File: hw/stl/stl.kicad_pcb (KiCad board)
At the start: 2 copper layers, 36 parts, among them Q1 IRF4905, Q2 5505, Q3 5505, Q4 5505, Q5 5505, Q6 5505, Q7 5505, Q8 5505, Q9 5505, U1 STM8S003F3P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

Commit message: WIP: tracing in progress
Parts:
- removed OUT1: Screw_Terminal_01x05, TerminalBlock_MetzConnect:TerminalBlock_MetzConnect_Type011_RT05505HBWC_1x05_P5.00mm_Horizontal
- removed Q5, Q9: 5505, Package_TO_SOT_SMD:TO-252-2
- removed R10, R14: 1K, Resistor_SMD:R_1206_3216Metric
- added D2: LED, LED_SMD:LED_1206_3216Metric, F.Cu at (216.9, 41.8)
- added J1: Screw_Terminal_01x04, TerminalBlock_Phoenix:TerminalBlock_Phoenix_MKDS-1,5-4_1x04_P5.00mm_Horizontal, F.Cu at (270.6, 27.8)
- added R15: 68, Resistor_SMD:R_1206_3216Metric, B.Cu at (221.4, 37.8)
- C1, C2, C3, C4, C5, Q4, Q7, R1, R11, R12, R13, R2, R3, R4, R6, U2: moved to B.Cu
- Q2: value 5505 -> IRFR5505TRLPBF; moved to B.Cu
- moved Q4 116.4 mm to (254.0, 46.7)
- moved Q2 104.7 mm to (254.0, 29.0)
- moved R12 96.1 mm to (245.5, 36.8), turned to 90 degrees
- moved SWIM1 93.1 mm to (210.6, 21.0)
- moved R8 92.0 mm to (245.5, 38.7), turned to 270 degrees
- moved R13 87.8 mm to (245.5, 45.8), turned to 90 degrees
- moved U2 83.9 mm to (200.4, 31.0), turned to 90 degrees
- moved Q3 83.5 mm to (254.0, 37.8)
- moved R2 82.9 mm to (225.4, 23.7)
- moved Q7 82.9 mm to (254.0, 37.7)
- moved C5 82.6 mm to (206.9, 32.1), turned to 270 degrees
- moved R6 81.3 mm to (220.0, 33.9), turned to 90 degrees
- moved R7 71.4 mm to (245.5, 30.0), turned to 270 degrees
- moved Q6 71.1 mm to (254.0, 29.1)
- moved Q1 68.7 mm to (199.4, 35.1)
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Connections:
- Q2 pad 1: +12V -> lamp2_ctrl
- Q2 pad 2: lamp2_ctrl -> lamp2_out
- Q2 pad 3: lamp2_out -> +12V
- Q3 pad 1: +12V -> lamp3_ctrl
- Q3 pad 2: lamp3_ctrl -> lamp3_out
- Q3 pad 3: lamp3_out -> +12V
- Q4 pad 1: +12V -> lamp4_ctrl
- Q4 pad 2: lamp4_ctrl -> lamp4_out
- Q4 pad 3: lamp4_out -> +12V
- Q6 pad 1: +12V -> lamp2_ctrl
- Q6 pad 2: lamp2_ctrl -> lamp2_out
- Q6 pad 3: lamp2_out -> +12V
- Q7 pad 1: +12V -> lamp3_ctrl
- Q7 pad 2: lamp3_ctrl -> lamp3_out
- Q7 pad 3: lamp3_out -> +12V
- Q8 pad 1: +12V -> lamp4_ctrl
- Q8 pad 2: lamp4_ctrl -> lamp4_out
- Q8 pad 3: lamp4_out -> +12V
- U1 pad 10: HEART_BEAT -> Net-(D2-Pad2)
- U1 pad 16: L5_STM_OUT -> Net-(U1-Pad16)
- U3 pad 1: L2_STM_OUT -> L4_STM_OUT
- U3 pad 11: Net-(U3-Pad11) -> lamp4_ctrl
- U3 pad 12: Net-(U3-Pad12) -> lamp4_ctrl
- U3 pad 13: lamp5_ctrl -> lamp3_ctrl
- U3 pad 14: lamp4_ctrl -> lamp3_ctrl
- U3 pad 15: lamp3_ctrl -> lamp2_ctrl
- U3 pad 2: L3_STM_OUT -> L4_STM_OUT
- U3 pad 3: L4_STM_OUT -> L3_STM_OUT
- U3 pad 4: L5_STM_OUT -> L3_STM_OUT
- U3 pad 5: GND -> L2_STM_OUT
- U3 pad 6: GND -> L2_STM_OUT
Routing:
- net +3V3: track 0.00 -> 14.1 mm, vias 0 -> 1
- net L4_STM_OUT: track 0.00 -> 12.7 mm
- net L3_STM_OUT: track 0.00 -> 12.5 mm
- net L2_STM_OUT: track 0.00 -> 11.7 mm
- net lamp2_ctrl: track 0.00 -> 11.2 mm
- net lamp4_ctrl: track 0.00 -> 11.1 mm
- net lamp3_ctrl: track 0.00 -> 11.1 mm
- net LEARN: track 0.00 -> 9.13 mm
- net Net-(D2-Pad1): track 0.00 -> 7.39 mm, vias 0 -> 1
- net Net-(C1-Pad2): track 0.00 -> 5.58 mm, vias 0 -> 1
- net Net-(D2-Pad2): track 0.00 -> 3.56 mm
- net CNT1: track 0.00 -> 2.96 mm, vias 0 -> 1
- net CNT2: track 0.00 -> 2.94 mm, vias 0 -> 1
- net NRST: track 0.00 -> 2.71 mm
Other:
- net class signalling added: clearance 0.2, trace_width 0.5, via_dia 0.8, via_drill 0.4

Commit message: WIP: draft tracing
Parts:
- moved R2 5.98 mm to (231.1, 25.3), turned to 180 degrees
- moved R1 5.97 mm to (225.4, 25.3), turned to 180 degrees
- moved J1 5.67 mm to (266.3, 24.2)
- moved R11 5.67 mm to (241.1, 24.5)
- moved R12 5.67 mm to (241.1, 33.2)
- moved R13 5.67 mm to (241.1, 42.2)
- moved R7 5.67 mm to (241.1, 26.4)
- moved R8 5.67 mm to (241.1, 35.1)
- moved R9 5.67 mm to (241.1, 44.0)
- moved Q2 5.67 mm to (249.6, 25.3)
- moved Q3 5.67 mm to (249.6, 34.2)
- moved Q4 5.67 mm to (249.6, 43.1)
- moved Q6 5.67 mm to (249.6, 25.5)
- moved Q7 5.67 mm to (249.6, 34.1)
- moved Q8 5.67 mm to (249.6, 43.1)
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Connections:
- C4 pad 1: Net-(C4-Pad1) -> +12V
- D1 pad 1: Net-(C4-Pad1) -> +12V
- IN1 pad 1: +12V -> +BATT
- J1 pad 1: +12V -> +BATT
- Q1 pad 2: +12V -> +BATT
- Q1 pad 3: Net-(C4-Pad1) -> +12V
- U2 pad 3: Net-(C4-Pad1) -> +12V
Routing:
- net +BATT: track 0.00 -> 143.4 mm
- net +12V: track 0.00 -> 46.8 mm, vias 0 -> 18
- net lamp4_out: track 0.00 -> 32.3 mm
- net lamp2_out: track 0.00 -> 32.2 mm
- net lamp3_out: track 0.00 -> 29.1 mm
- net +3V3: track 14.1 -> 42.5 mm, vias 1 -> 0
- net CNT2: track 2.94 -> 29.7 mm, vias 1 -> 3
- net CNT1: track 2.96 -> 24.4 mm
- net lamp2_ctrl: track 11.2 -> 32.3 mm, vias 0 -> 1
- net SWIM: track 0.00 -> 19.3 mm, vias 0 -> 1
- net lamp4_ctrl: track 11.1 -> 27.7 mm, vias 0 -> 1
- net NRST: track 2.71 -> 18.9 mm
- net lamp3_ctrl: track 11.1 -> 27.0 mm, vias 0 -> 1
- added copper zone on B.Cu, net +12V
- added copper zone on F.Cu, net +12V
- added copper zone on B.Cu, net GND
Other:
- board outline added: 102 x 43.8 mm
- net class 12V added: clearance 0.2, trace_width 0.5, via_dia 0.8, via_drill 0.4
- net class 3v3 added: clearance 0.2, trace_width 0.5, via_dia 0.8, via_drill 0.4
- net class lamp added: clearance 0.2, trace_width 2, via_dia 0.8, via_drill 0.4
- net class signalling removed
- net class signals added: clearance 0.2, trace_width 0.3, via_dia 0.8, via_drill 0.4

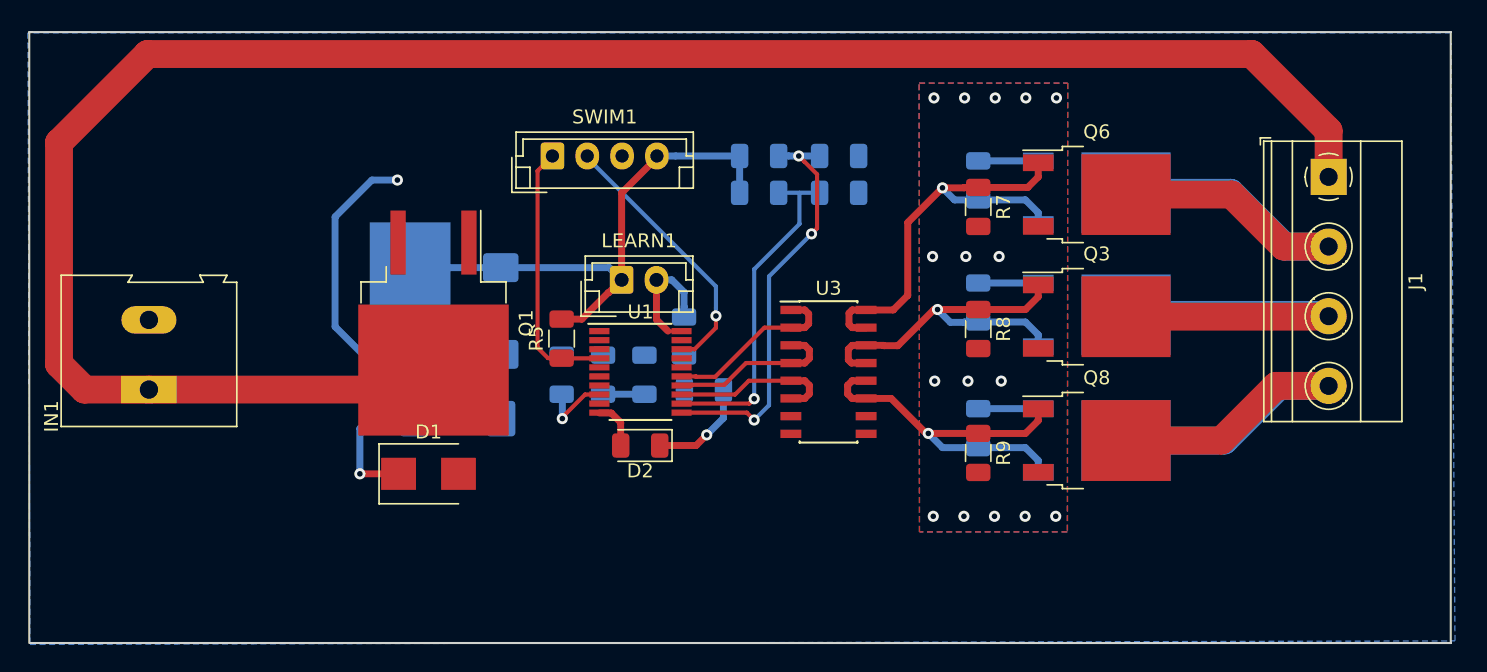
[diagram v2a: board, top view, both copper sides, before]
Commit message: [FEAT]: pcb is traced, v2.0
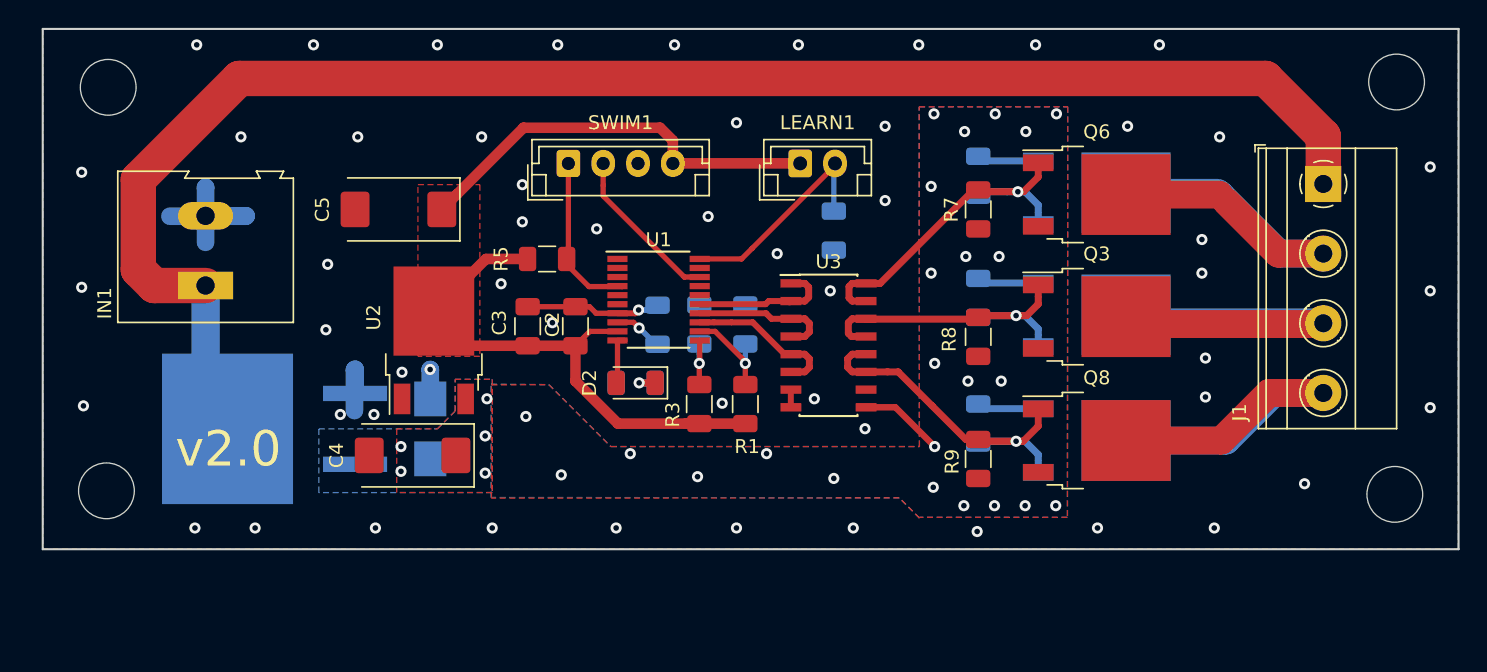
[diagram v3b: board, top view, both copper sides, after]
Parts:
- added REF**: MountingHole_4mm, MountingHole:MountingHole_4mm, F.Cu at (178.7, 17.8)
- added REF**: MountingHole_4mm, MountingHole:MountingHole_4mm, F.Cu at (178.6, 46.7)
- added REF**: MountingHole_4mm, MountingHole:MountingHole_4mm, F.Cu at (271.1, 17.4)
- added REF**: MountingHole_4mm, MountingHole:MountingHole_4mm, F.Cu at (271.0, 47.0)
- C2, C3, C4, C5, R1, R3, U2: moved to F.Cu
- D1, Q1: moved to B.Cu
- moved R3 18.3 mm to (221.1, 40.5), turned to 270 degrees
- moved R4 15.7 mm to (221.1, 34.8), turned to 270 degrees
- moved LEARN1 15.3 mm to (228.3, 23.2)
- moved R1 15.2 mm to (224.4, 40.5), turned to 270 degrees
- moved Q1 13.7 mm to (190.6, 42.3), turned to 180 degrees
- moved R6 13.2 mm to (230.8, 28.1)
- moved R2 11.6 mm to (224.4, 34.8), turned to 270 degrees
- moved C5 10.3 mm to (199.5, 26.5), turned to 180 degrees
- moved IN1 8.50 mm to (185.7, 32.0)
- moved C1 7.76 mm to (218.1, 34.8)
- moved C3 6.43 mm to (208.8, 34.9)
- moved C2 6.05 mm to (212.2, 34.9)
- moved R5 5.81 mm to (210.2, 30.1), turned to 180 degrees
- moved U1 5.34 mm to (218.2, 33.0)
- moved R15 4.93 mm to (216.5, 39.0)
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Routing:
- net GND: track 0.00 -> 30.2 mm, vias 0 -> 56
- net +3V3: track 42.5 -> 71.3 mm
- net +12V: track 46.8 -> 19.0 mm, vias 18 -> 29
- net +BATT: track 143.4 -> 115.9 mm
- net CNT2: track 29.7 -> 4.57 mm, vias 3 -> 1
- net CNT1: track 24.4 -> 7.25 mm
- net SWIM: track 19.3 -> 11.7 mm, vias 1 -> 0
- net LEARN: track 9.13 -> 16.6 mm
- net lamp2_ctrl: track 32.3 -> 26.2 mm
- net NRST: track 18.9 -> 12.9 mm
- net Net-(D2-Pad1): track 7.39 -> 2.29 mm
- net lamp3_ctrl: track 27.0 -> 23.7 mm
- net L4_STM_OUT: track 12.8 -> 10.3 mm
- net lamp4_ctrl: track 27.7 -> 25.7 mm
- net Net-(C1-Pad2): track 5.25 -> 3.35 mm
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- added copper zone on F.Cu, net +3V3
- added copper zone on F.Cu, net GND
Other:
- board size 102 x 43.8 mm -> 101.6 x 37.3 mm
- board text added: "v2.0"

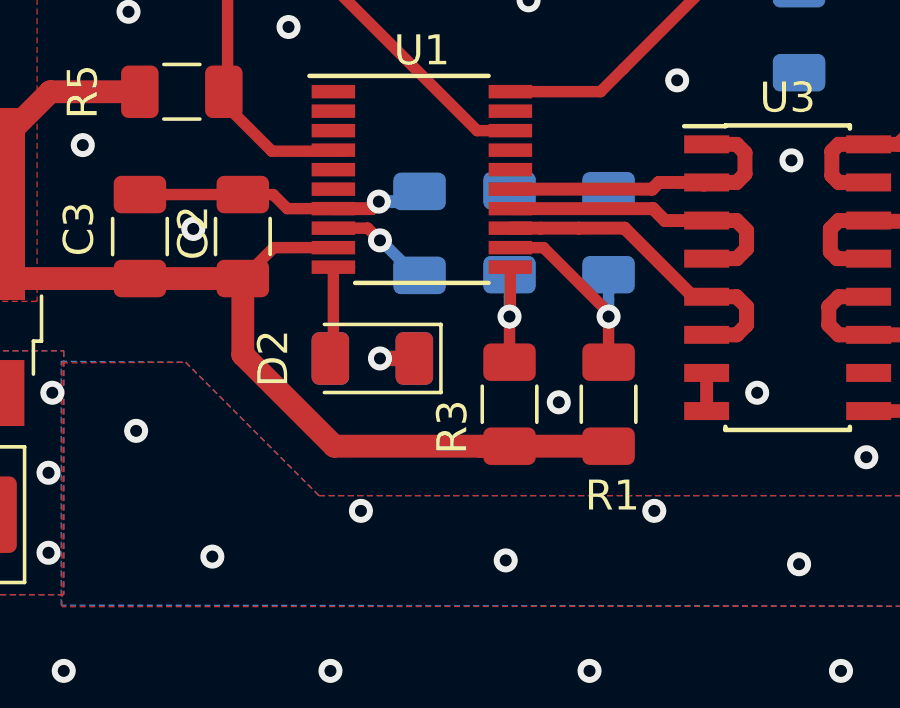
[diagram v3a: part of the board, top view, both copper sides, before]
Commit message: [FEAT]: resistors R1-R4 moved together
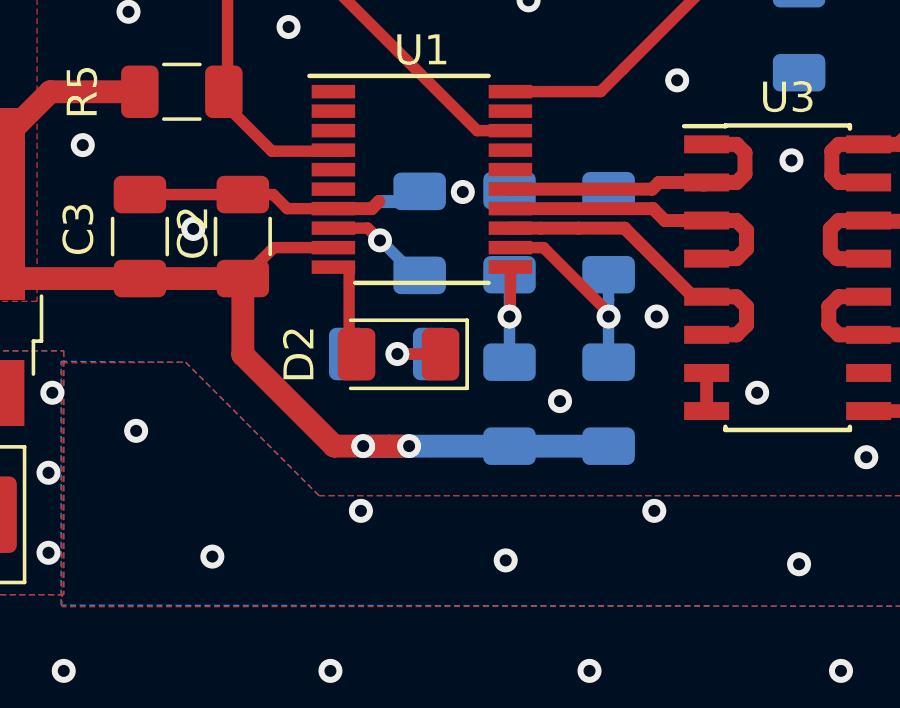
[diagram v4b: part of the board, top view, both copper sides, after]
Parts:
- R1, R3: moved to B.Cu
- moved D2 0.89 mm to (217.4, 38.9)
- moved R15 0.60 mm to (217.1, 38.8)
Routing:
- net +3V3: track 71.3 -> 72.8 mm, vias 0 -> 2
- net GND: vias 56 -> 57

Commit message: [FEAT]: edited missed via
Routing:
- net GND: vias 57 -> 58
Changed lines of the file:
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@@
     (thickness 1.6)
     (drawings 5)
-    (tracks 294)
+    (tracks 296)
     (zones 0)
     (modules 38)
@@
     (35 F.Paste user hide)
     (36 B.SilkS user hide)
-    (37 F.SilkS user hide)
+    (37 F.SilkS user)
     (38 B.Mask user hide)
     (39 F.Mask user hide)
@@
   (segment (start 217.77 33.76) (end 218.11 33.42) (width 0.4318) (layer B.Cu) (net 5))
   (segment (start 216.75 33.76) (end 217.77 33.76) (width 0.4318) (layer B.Cu) (net 5))
+  (via (at 226.01 37.59) (size 0.8) (drill 0.4) (layers F.Cu B.Cu) (net 5))
+  (via (at 222.79 40.41) (size 0.8) (drill 0.4) (layers F.Cu B.Cu) (net 5))
+  (segment (start 216.75 33.76) (end 216.75 33.76) (width 0.4318) (layer F.Cu) (net 5))
+  (via (at 216.75 33.76) (size 0.8) (drill 0.4) (layers F.Cu B.Cu) (net 5))
   (segment (start 216.515 33.995) (end 216.75 33.76) (width 0.4318) (layer F.Cu) (net 5))
   (segment (start 215.236 33.995) (end 216.515 33.995) (width 0.4318) (layer F.Cu) (net 5))
-  (via (at 226.01 37.59) (size 0.8) (drill 0.4) (layers F.Cu B.Cu) (net 5))
-  (via (at 222.79 40.41) (size 0.8) (drill 0.4) (layers F.Cu B.Cu) (net 5))
   (segment (start 221.107 36.198) (end 221.107001 36.923001) (width 0.381) (layer B.Cu) (net 6))
   (segment (start 221.107001 36.923001) (end 221.107001 37.465001) (width 0.381) (layer B.Cu) (net 6))

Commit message: Some writings, adds gerbers
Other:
- board text added: "+"
- board text added: "-"
- board text added: "1"
- board text added: "2"
- board text added: "2020"
- board text added: "3"
- board text added: "4"
- board text added: "Fox + Urx"
- board text added: "SWIM"
- board text added: "nRST"
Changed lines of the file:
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@@
-(kicad_pcb (version 20171130) (host pcbnew "(5.1.4)-1")
+(kicad_pcb (version 20171130) (host pcbnew "(5.1.4-0)")
   (general
     (thickness 1.6)
-    (drawings 5)
+    (drawings 18)
     (tracks 296)
     (zones 0)
@@
     (0 F.Cu signal)
     (31 B.Cu signal)
-    (32 B.Adhes user hide)
+    (32 B.Adhes user)
     (33 F.Adhes user)
-    (34 B.Paste user hide)
-    (35 F.Paste user hide)
-    (36 B.SilkS user hide)
+    (34 B.Paste user)
+    (35 F.Paste user)
+    (36 B.SilkS user)
     (37 F.SilkS user)
-    (38 B.Mask user hide)
-    (39 F.Mask user hide)
+    (38 B.Mask user)
+    (39 F.Mask user)
     (40 Dwgs.User user)
     (41 Cmts.User user)
@@
     (43 Eco2.User user)
     (44 Edge.Cuts user)
-    (45 Margin user hide)
+    (45 Margin user)
     (46 B.CrtYd user)
     (47 F.CrtYd user)
-    (48 B.Fab user hide)
-    (49 F.Fab user hide)
+    (48 B.Fab user)
+    (49 F.Fab user)
   )
   (setup
-    (last_trace_width 0.381)
+    (last_trace_width 0.25)
     (user_trace_width 0.254)
     (user_trace_width 0.381)
@@
     (visible_elements 7FFFFFFF)
     (pcbplotparams
-      (layerselection 0x010fc_ffffffff)
+      (layerselection 0x010f0_ffffffff)
       (usegerberextensions false)
       (usegerberattributes false)
-      (usegerberadvancedattributes false)
+      (usegerberadvancedattributes true)
       (creategerberjobfile false)
-      (excludeedgelayer true)
+      (excludeedgelayer false)
       (linewidth 0.100000)
       (plotframeref false)
       (viasonmask false)
       (mode 1)
-      (useauxorigin false)
+      (useauxorigin true)
       (hpglpennumber 1)
       (hpglpenspeed 20)
@@
       (plotvalue true)
       (plotinvisibletext false)
-      (padsonsilk false)
+      (padsonsilk true)
       (subtractmaskfromsilk false)
       (outputformat 1)
       (mirror false)
-      (drillshape 1)
+      (drillshape 0)
       (scaleselection 1)
-      (outputdirectory ""))
+      (outputdirectory "plots/"))
   )
   (net 0 "")
@@
     (tags resistor)
     (attr smd)
-    (fp_text reference R15 (at -0.195 -1.961) (layer B.SilkS)
+    (fp_text reference R15 (at 3.3994 -0.0484 90) (layer B.SilkS)
       (effects (font (size 1 1) (thickness 0.15)) (justify mirror))
     )
@@
     (descr "JST EH series connector, B04B-EH-A (http://www.jst-mfg.com/product/pdf/eng/eEH.pdf), generated with kicad-footprint-generator")
     (tags "connector JST EH side entry")
-    (fp_text reference SWIM1 (at 3.75 -2.921) (layer F.SilkS)
+    (fp_text reference SWIM1 (at 3.7338 3.2512) (layer F.SilkS)
       (effects (font (size 1 1) (thickness 0.15)))
     )
@@
     (tags resistor)
     (attr smd)
-    (fp_text reference R13 (at 0 1.82 90) (layer B.SilkS)
+    (fp_text reference R13 (at 0 -2.1336 90) (layer B.SilkS)
       (effects (font (size 1 1) (thickness 0.15)) (justify mirror))
     )
@@
     (tags resistor)
     (attr smd)
-    (fp_text reference R12 (at 0 1.82 90) (layer B.SilkS)
+    (fp_text reference R12 (at 0.0254 -2.1336 90) (layer B.SilkS)
       (effects (font (size 1 1) (thickness 0.15)) (justify mirror))
     )
@@
     (tags resistor)
     (attr smd)
-    (fp_text reference R11 (at 0 1.82 90) (layer B.SilkS)
+    (fp_text reference R11 (at 0 -2.1336 90) (layer B.SilkS)
       (effects (font (size 1 1) (thickness 0.15)) (justify mirror))
     )
@@
     (descr "Altech AK300 terminal block, pitch 5.0mm, 45 degree angled, see http://www.mouser.com/ds/2/16/PCBMETRC-24178.pdf")
     (tags "Altech AK300 terminal block pitch 5.0mm")
-    (fp_text reference IN1 (at -1.27 -7.239 90) (layer F.SilkS)
+    (fp_text reference IN1 (at -3.429 0.1778 180) (layer F.SilkS)
       (effects (font (size 1 1) (thickness 0.15)))
     )
@@
     )
   )
+  (gr_text 2020 (at 196.6468 20.2438) (layer B.SilkS)
+    (effects (font (size 1 1) (thickness 0.15)) (justify mirror))
+  )
+  (gr_line (start 192.024 19.2191) (end 201.2696 19.2191) (layer B.SilkS) (width 0.15))
+  (gr_text "Fox + Urx" (at 196.6468 18.0594) (layer B.SilkS)
+    (effects (font (size 1 1) (thickness 0.15)) (justify mirror))
+  )
+  (gr_text nRST (at 211.6415 19.7104 90) (layer F.SilkS)
+    (effects (font (size 1 1) (thickness 0.15)))
+  )
+  (gr_text SWIM (at 214.1415 19.662781 90) (layer F.SilkS)
+    (effects (font (size 1 1) (thickness 0.15)))
+  )
+  (gr_text - (at 216.6415 20.900877 90) (layer F.SilkS)
+    (effects (font (size 1 1) (thickness 0.15)))
+  )
+  (gr_text + (at 219.209 20.702424) (layer F.SilkS)
+    (effects (font (size 1 1) (thickness 0.15)))
+  )
+  (gr_text 4 (at 272.161 39.714201 90) (layer F.SilkS)
+    (effects (font (size 1 1) (thickness 0.15)))
+  )
+  (gr_text 3 (at 272.161 34.714201 90) (layer F.SilkS)
+    (effects (font (size 1 1) (thickness 0.15)))
+  )
+  (gr_text 2 (at 272.161 29.714201 90) (layer F.SilkS)
+    (effects (font (size 1 1) (thickness 0.15)))
+  )
+  (gr_text 1 (at 272.161 24.714201 90) (layer F.SilkS)
+    (effects (font (size 1 1) (thickness 0.15)))
+  )
+  (gr_text - (at 177.6222 26.8986 90) (layer F.SilkS)
+    (effects (font (size 3 3) (thickness 0.15)))
+  )
+  (gr_text + (at 177.927 31.9024) (layer F.SilkS)
+    (effects (font (size 3 3) (thickness 0.3)) (justify mirror))
+  )
   (gr_text "v2.0\n" (at 187.31 43.74) (layer F.SilkS)
